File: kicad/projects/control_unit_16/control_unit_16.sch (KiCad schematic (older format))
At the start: 57 parts, among them J1 Conn_01x04_Female, J2 Control_signal_backplane, J3 Bus_connection, J4 Aux_connection, J5 Conn_01x16_Female, J6 LED_CONTROL, J7 TOP_POWER, U1 74HC04, U10 28C256, U11 28C256, U2 28C256, U3 74HC173, U4 74HC377, U5 74HC161, U6 28C256, U7 74HC245, U8 74HC245, U9 74HC138

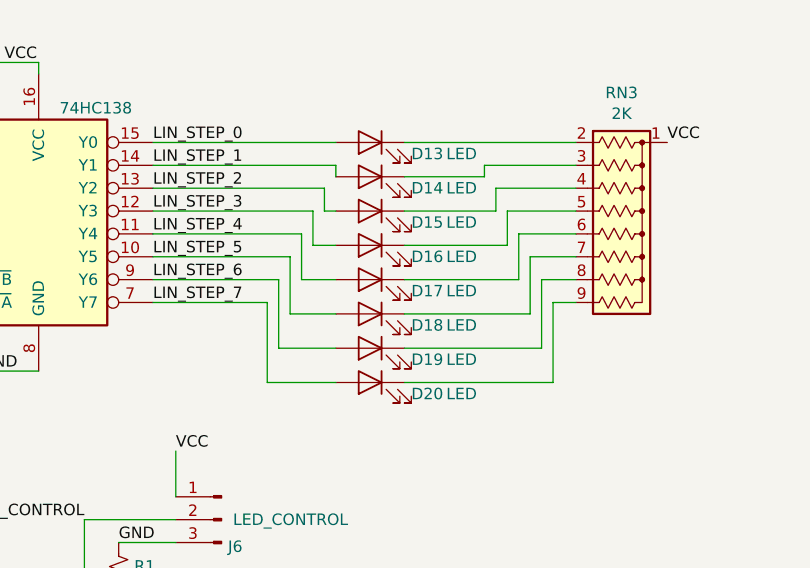
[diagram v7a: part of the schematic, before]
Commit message: Fix reversed microcode step LEDs in Control unit. Some register16 git tracking wierdness...
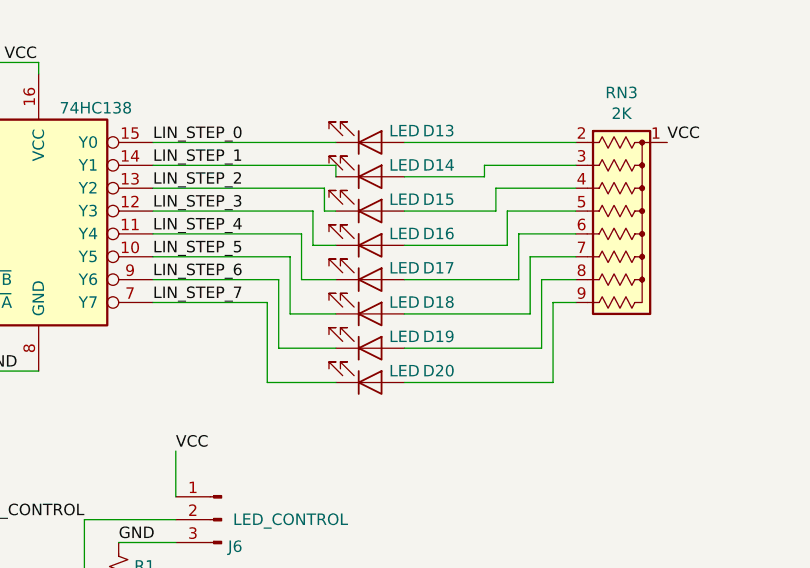
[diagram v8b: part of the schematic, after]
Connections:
- net LIN_STEP_0: now also D13.1 (K); no longer D13.2 (A)
- net LIN_STEP_1: now also D14.1 (K); no longer D14.2 (A)
- net LIN_STEP_2: now also D15.1 (K); no longer D15.2 (A)
- net LIN_STEP_3: now also D16.1 (K); no longer D16.2 (A)
- net LIN_STEP_4: now also D17.1 (K); no longer D17.2 (A)
- net LIN_STEP_5: now also D18.1 (K); no longer D18.2 (A)
- net LIN_STEP_6: now also D19.1 (K); no longer D19.2 (A)
- net LIN_STEP_7: now also D20.1 (K); no longer D20.2 (A)
- net at RN3.9 (R8): now also D20.2 (A); no longer D20.1 (K)
- net at RN3.8 (R7): now also D19.2 (A); no longer D19.1 (K)
- net at RN3.7 (R6): now also D18.2 (A); no longer D18.1 (K)
- net at RN3.6 (R5): now also D17.2 (A); no longer D17.1 (K)
- net at RN3.5 (R4): now also D16.2 (A); no longer D16.1 (K)
- net at RN3.4 (R3): now also D15.2 (A); no longer D15.1 (K)
- net at RN3.3 (R2): now also D14.2 (A); no longer D14.1 (K)
- net at RN3.2 (R1): now also D13.2 (A); no longer D13.1 (K)
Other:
- moved on the sheet: D13, D14, D15, D16, D17, D18, D19, D20
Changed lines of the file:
@@
-$EndComp
-$Comp
-L Device:LED D20
-U 1 1 5FD956D3
-P 6700 2150
-F 0 "D20" H 6450 2100 50  0000 C CNN
-F 1 "LED" H 6300 2100 50  0000 C CNN
-F 2 "sixteen-bit-computer:LED_D5.0mm_Horizontal_O3.81mm_Z3.0mm" H 6700 2150 50  0001 C CNN
-F 3 "~" H 6700 2150 50  0001 C CNN
-	1    6700 2150
-	-1   0    0    -1
-$EndComp
-$Comp
-L Device:LED D19
-U 1 1 5FD96F8F
-P 6700 2000
-F 0 "D19" H 6450 1950 50  0000 C CNN
-F 1 "LED" H 6300 1950 50  0000 C CNN
-F 2 "sixteen-bit-computer:LED_D5.0mm_Horizontal_O3.81mm_Z3.0mm" H 6700 2000 50  0001 C CNN
-F 3 "~" H 6700 2000 50  0001 C CNN
-	1    6700 2000
-	-1   0    0    -1
-$EndComp
-$Comp
-L Device:LED D18
-U 1 1 5FD994D8
-P 6700 1850
-F 0 "D18" H 6450 1800 50  0000 C CNN
-F 1 "LED" H 6300 1800 50  0000 C CNN
-F 2 "sixteen-bit-computer:LED_D5.0mm_Horizontal_O3.81mm_Z3.0mm" H 6700 1850 50  0001 C CNN
-F 3 "~" H 6700 1850 50  0001 C CNN
-	1    6700 1850
-	-1   0    0    -1
-$EndComp
-$Comp
-L Device:LED D17
-U 1 1 5FD994E2
-P 6700 1700
-F 0 "D17" H 6450 1650 50  0000 C CNN
-F 1 "LED" H 6300 1650 50  0000 C CNN
-F 2 "sixteen-bit-computer:LED_D5.0mm_Horizontal_O3.81mm_Z3.0mm" H 6700 1700 50  0001 C CNN
-F 3 "~" H 6700 1700 50  0001 C CNN
-	1    6700 1700
-	-1   0    0    -1
-$EndComp
-$Comp
-L Device:LED D16
-U 1 1 5FD9D16A
-P 6700 1550
-F 0 "D16" H 6450 1500 50  0000 C CNN
-F 1 "LED" H 6300 1500 50  0000 C CNN
-F 2 "sixteen-bit-computer:LED_D5.0mm_Horizontal_O3.81mm_Z3.0mm" H 6700 1550 50  0001 C CNN
-F 3 "~" H 6700 1550 50  0001 C CNN
-	1    6700 1550
-	-1   0    0    -1
-$EndComp
-$Comp
-L Device:LED D15
-U 1 1 5FD9D170
-P 6700 1400
-F 0 "D15" H 6450 1350 50  0000 C CNN
-F 1 "LED" H 6300 1350 50  0000 C CNN
-F 2 "sixteen-bit-computer:LED_D5.0mm_Horizontal_O3.81mm_Z3.0mm" H 6700 1400 50  0001 C CNN
-F 3 "~" H 6700 1400 50  0001 C CNN
-	1    6700 1400
-	-1   0    0    -1
-$EndComp
-$Comp
-L Device:LED D14
-U 1 1 5FD9D176
-P 6700 1250
-F 0 "D14" H 6450 1200 50  0000 C CNN
-F 1 "LED" H 6300 1200 50  0000 C CNN
-F 2 "sixteen-bit-computer:LED_D5.0mm_Horizontal_O3.81mm_Z3.0mm" H 6700 1250 50  0001 C CNN
-F 3 "~" H 6700 1250 50  0001 C CNN
-	1    6700 1250
-	-1   0    0    -1
-$EndComp
-$Comp
-L Device:LED D13
-U 1 1 5FD9D17C
-P 6700 1100
-F 0 "D13" H 6450 1050 50  0000 C CNN
-F 1 "LED" H 6300 1050 50  0000 C CNN
-F 2 "sixteen-bit-computer:LED_D5.0mm_Horizontal_O3.81mm_Z3.0mm" H 6700 1100 50  0001 C CNN
-F 3 "~" H 6700 1100 50  0001 C CNN
-	1    6700 1100
-	-1   0    0    -1
 $EndComp
 $Comp
@@
 Wire Wire Line
 	5400 7100 6050 7100
+$Comp
+L Device:LED D20
+U 1 1 5FD956D3
+P 6700 2150
+F 0 "D20" H 7000 2100 50  0000 C CNN
+F 1 "LED" H 6850 2100 50  0000 C CNN
+F 2 "sixteen-bit-computer:LED_D5.0mm_Horizontal_O3.81mm_Z3.0mm" H 6700 2150 50  0001 C CNN
+F 3 "~" H 6700 2150 50  0001 C CNN
+	1    6700 2150
+	1    0    0    1
+$EndComp
+$Comp
+L Device:LED D19
+U 1 1 5FD96F8F
+P 6700 2000
+F 0 "D19" H 7000 1950 50  0000 C CNN
+F 1 "LED" H 6850 1950 50  0000 C CNN
+F 2 "sixteen-bit-computer:LED_D5.0mm_Horizontal_O3.81mm_Z3.0mm" H 6700 2000 50  0001 C CNN
+F 3 "~" H 6700 2000 50  0001 C CNN
+	1    6700 2000
+	1    0    0    1
+$EndComp
+$Comp
+L Device:LED D18
+U 1 1 5FD994D8
+P 6700 1850
+F 0 "D18" H 7000 1800 50  0000 C CNN
+F 1 "LED" H 6850 1800 50  0000 C CNN
+F 2 "sixteen-bit-computer:LED_D5.0mm_Horizontal_O3.81mm_Z3.0mm" H 6700 1850 50  0001 C CNN
+F 3 "~" H 6700 1850 50  0001 C CNN
+	1    6700 1850
+	1    0    0    1
+$EndComp
+$Comp
+L Device:LED D17
+U 1 1 5FD994E2
+P 6700 1700
+F 0 "D17" H 7000 1650 50  0000 C CNN
+F 1 "LED" H 6850 1650 50  0000 C CNN
+F 2 "sixteen-bit-computer:LED_D5.0mm_Horizontal_O3.81mm_Z3.0mm" H 6700 1700 50  0001 C CNN
+F 3 "~" H 6700 1700 50  0001 C CNN
+	1    6700 1700
+	1    0    0    1
+$EndComp
+$Comp
+L Device:LED D16
+U 1 1 5FD9D16A
+P 6700 1550
+F 0 "D16" H 7000 1500 50  0000 C CNN
+F 1 "LED" H 6850 1500 50  0000 C CNN
+F 2 "sixteen-bit-computer:LED_D5.0mm_Horizontal_O3.81mm_Z3.0mm" H 6700 1550 50  0001 C CNN
+F 3 "~" H 6700 1550 50  0001 C CNN
+	1    6700 1550
+	1    0    0    1
+$EndComp
+$Comp
+L Device:LED D15
+U 1 1 5FD9D170
+P 6700 1400
+F 0 "D15" H 7000 1350 50  0000 C CNN
+F 1 "LED" H 6850 1350 50  0000 C CNN
+F 2 "sixteen-bit-computer:LED_D5.0mm_Horizontal_O3.81mm_Z3.0mm" H 6700 1400 50  0001 C CNN
+F 3 "~" H 6700 1400 50  0001 C CNN
+	1    6700 1400
+	1    0    0    1
+$EndComp
+$Comp
+L Device:LED D14
+U 1 1 5FD9D176
+P 6700 1250
+F 0 "D14" H 7000 1200 50  0000 C CNN
+F 1 "LED" H 6850 1200 50  0000 C CNN
+F 2 "sixteen-bit-computer:LED_D5.0mm_Horizontal_O3.81mm_Z3.0mm" H 6700 1250 50  0001 C CNN
+F 3 "~" H 6700 1250 50  0001 C CNN
+	1    6700 1250
+	1    0    0    1
+$EndComp
+$Comp
+L Device:LED D13
+U 1 1 5FD9D17C
+P 6700 1100
+F 0 "D13" H 7000 1050 50  0000 C CNN
+F 1 "LED" H 6850 1050 50  0000 C CNN
+F 2 "sixteen-bit-computer:LED_D5.0mm_Horizontal_O3.81mm_Z3.0mm" H 6700 1100 50  0001 C CNN
+F 3 "~" H 6700 1100 50  0001 C CNN
+	1    6700 1100
+	1    0    0    1
+$EndComp
 $EndSCHEMATC
